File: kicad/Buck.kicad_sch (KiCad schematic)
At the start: 12 parts, among them U11 TPS54331DR, U12 6.8uH

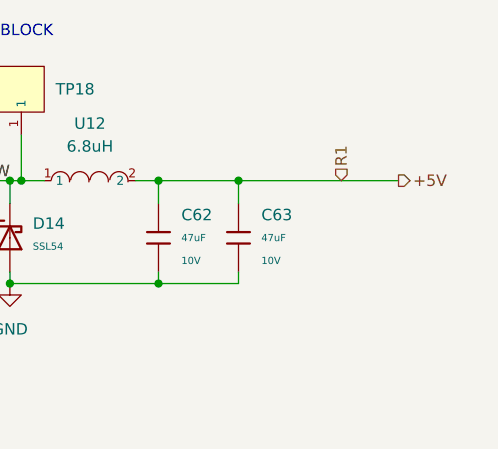
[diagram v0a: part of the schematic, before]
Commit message: Footprint routing completed
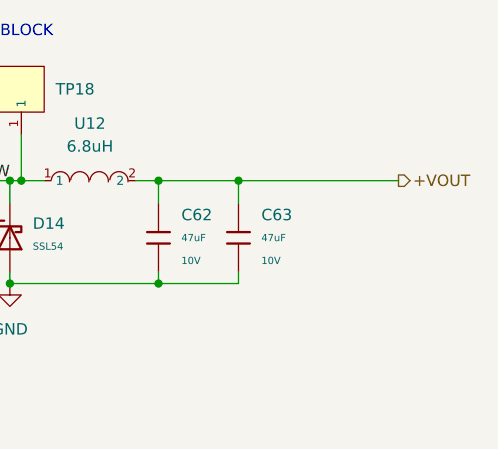
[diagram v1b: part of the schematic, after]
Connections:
- net +5V renamed +VOUT
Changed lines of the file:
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@@
 		)
 	)
-	(hierarchical_label "R1"
-		(shape input)
-		(at 190.5 66.04 90)
-		(effects
-			(font
-				(size 1.27 1.27)
-			)
-			(justify left)
-		)
-	)
-	(hierarchical_label "+5V"
+	(hierarchical_label "+VOUT"
 		(shape output)
 		(at 196.85 66.04 0)
